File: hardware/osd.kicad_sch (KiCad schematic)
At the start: 0 parts

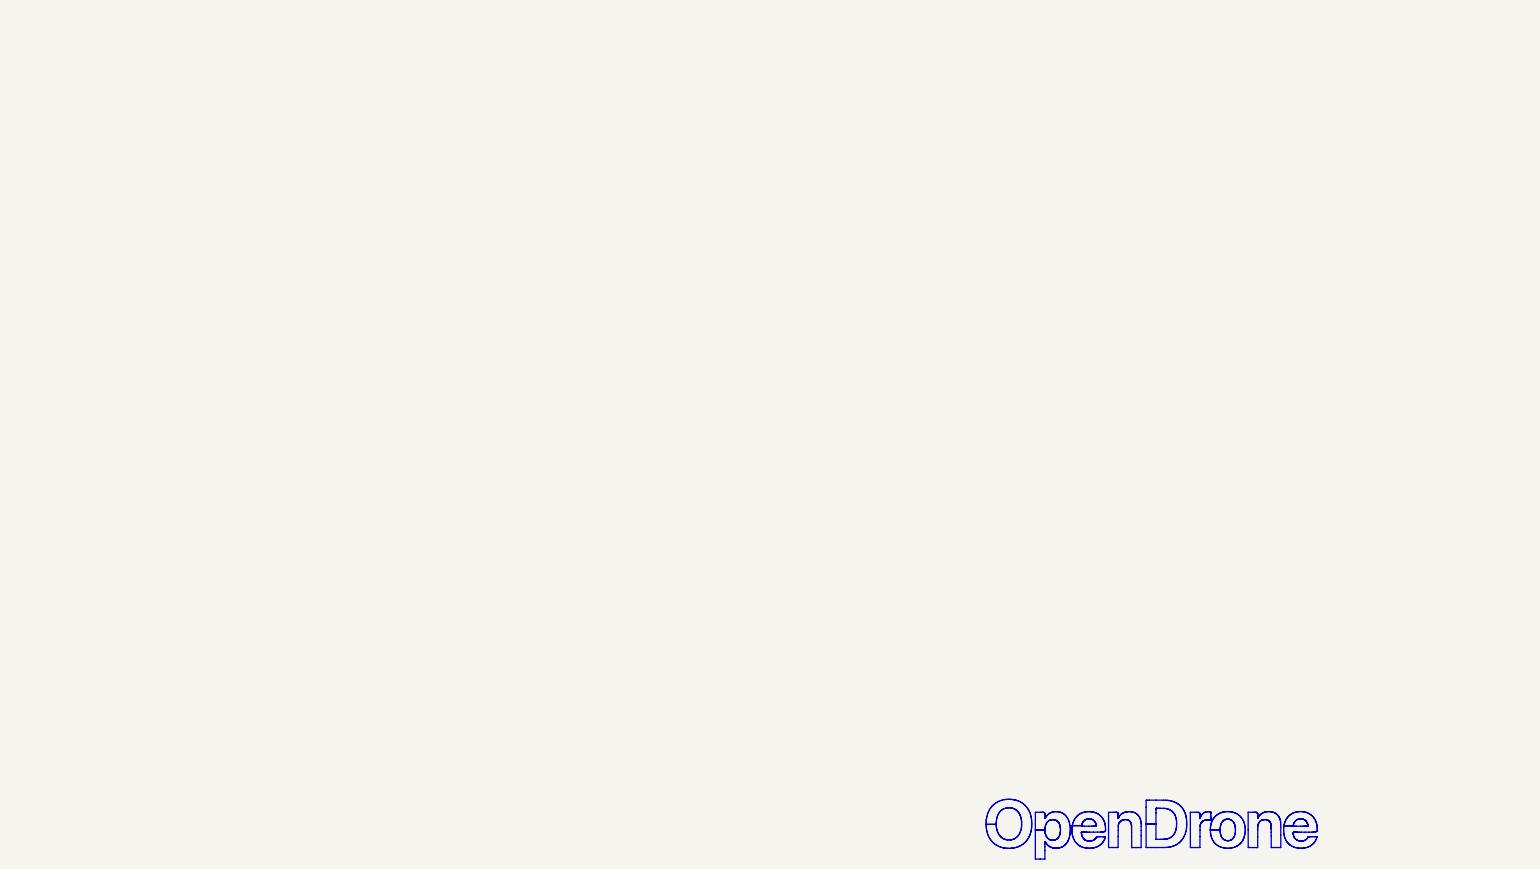
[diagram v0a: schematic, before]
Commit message: schematic: rx (ESP32-PICO-V3 + SX1281 + Wi-Fi antenna + boot button), blackbox and osd sheets drawn
Co-Authored-By: Claude Opus 5.5 <noreply@anthropic.com>
Claude-Session: https://claude.ai/code/session_01RFaS5jnC9tnPam9GBgmGnG
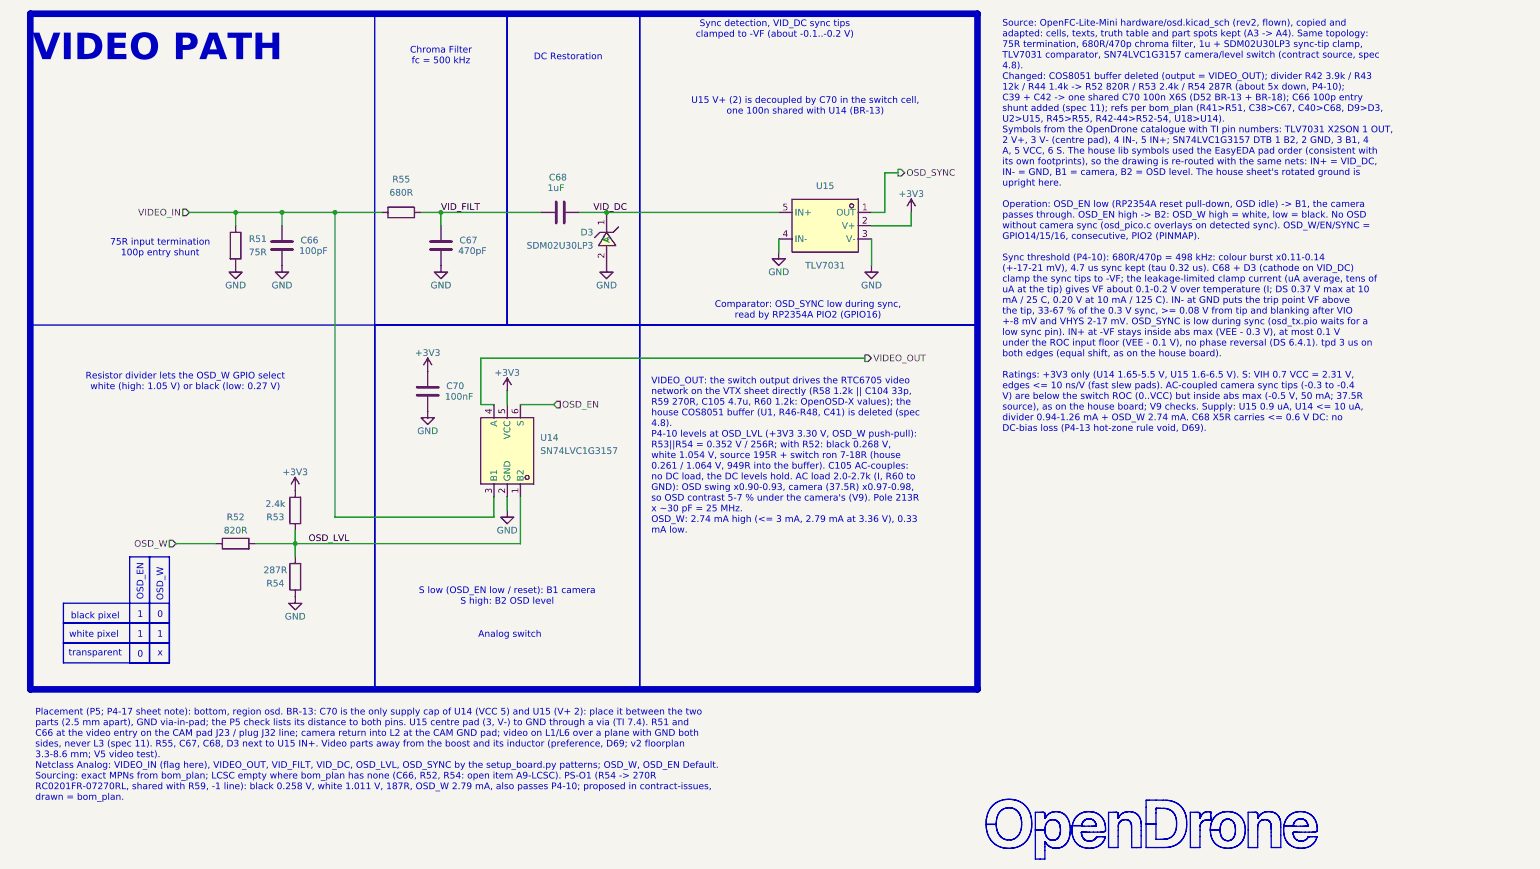
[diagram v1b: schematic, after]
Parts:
- added C66: 100pF, lib:C_0201_0603Metric_W, symbol Device:C
- added C67: 470pF, lib:C_0201_0603Metric_W, symbol Device:C
- added C68: 1uF, lib:C_0201_0603Metric_W, symbol Device:C
- added C70: 100nF, lib:C_0201_0603Metric_W, symbol Device:C
- added D3: SDM02U30LP3, lib:X3-DFN0603-2_L0.6-W0.3-RD_W, symbol OpenDrone:SDM02U30LP3-7B
- added R51: 75R, lib:R_0201_0603Metric_W, symbol Device:R
- added R52: 820R, lib:R_0201_0603Metric_W, symbol Device:R
- added R53: 2.4k, lib:R_0201_0603Metric_W, symbol Device:R
- added R54: 287R, lib:R_0201_0603Metric_W, symbol Device:R
- added R55: 680R, lib:R_0201_0603Metric_W, symbol Device:R
- added U14: SN74LVC1G3157, lib:X2SON-6_L1.0-W0.8-BL_Dense, symbol OpenDrone:SN74LVC1G3157DTBR
- added U15: TLV7031, lib:X2SON-4_L0.8-W0.8-P0.48-TL-A_Dense, symbol OpenDrone:TLV7031DPWR
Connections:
- new net +3V3: C70.1, R53.2, U14.5 (VCC), U15.2 (V+)
- new net GND: C66.2, C67.2, C70.2, D3.2 (A), R51.2, R54.1, U14.2 (GND), U15.3 (V-), U15.4 (IN-)
- new net OSD_EN: U14.6 (S)
- new net OSD_LVL: R52.2, R53.1, R54.2, U14.1 (B2)
- new net OSD_SYNC: U15.1 (OUT)
- new net OSD_W: R52.1
- new net VIDEO_IN: C66.1, R51.1, R55.2, U14.3 (B1)
- new net VIDEO_OUT: U14.4 (A)
- new net VID_DC: C68.2, D3.1 (C), U15.5 (IN+)
- new net VID_FILT: C67.1, C68.1, R55.1
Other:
- note added: "0"
- note added: "1"
- note added: "75R input termination 100p entry shunt"
- note added: "Analog switch"
- note added: "Chroma Filter fc = 500 kHz"
- note added: "Comparator: OSD_SYNC low during sync, read by RP2354A PIO2 (GPIO16)"
- note added: "DC Restoration"
- note added: "OSD_EN"
- note added: "OSD_W"
- note added: "Resistor divider lets the OSD_W GPIO select white (high: 1.05 V) or black (low: 0.27 V)"
- note added: "S low (OSD_EN low / reset): B1 camera S high: B2 OSD level"
- note added: "Sync detection, VID_DC sync tips clamped to -VF (about -0.1..-0.2 V)"
- note added: "U15 V+ (2) is decoupled by C70 in the switch cell, one 100n shared with U14 (BR-13)"
- note added: "VIDEO PATH"
- note added: "black pixel"
- note added: "transparent"
- note added: "white pixel"
- note added: "x"

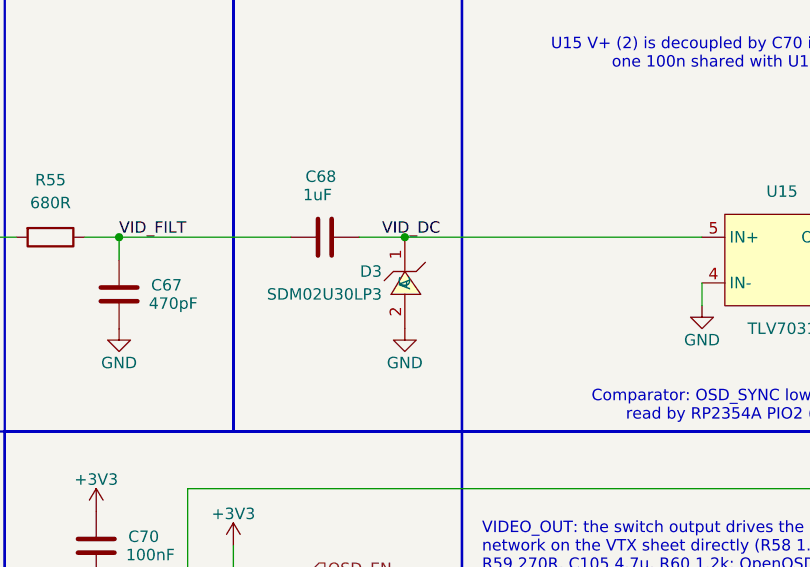
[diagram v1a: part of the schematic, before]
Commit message: wip: schematic integration in progress (saved after container restart)
Co-Authored-By: Claude Opus 5.5 <noreply@anthropic.com>
Claude-Session: https://claude.ai/code/session_01RFaS5jnC9tnPam9GBgmGnG
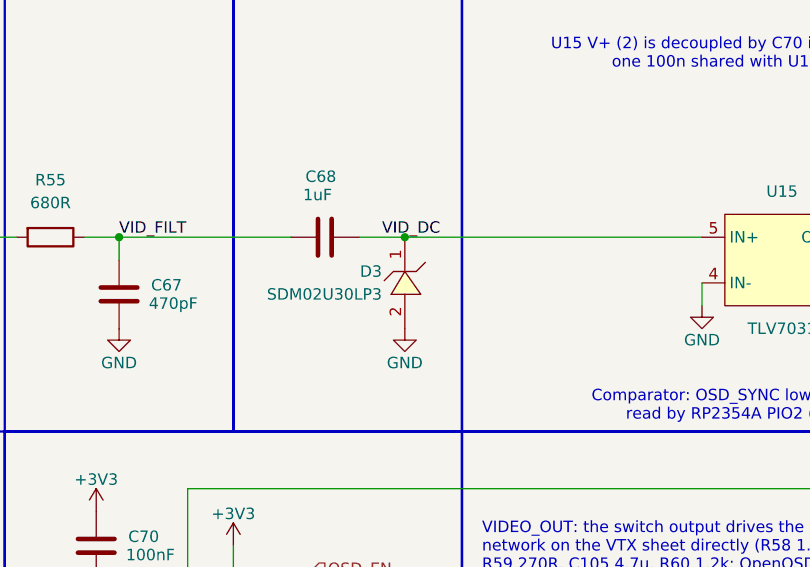
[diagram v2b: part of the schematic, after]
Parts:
- D3: symbol OpenDrone:SDM02U30LP3-7B -> lib:SDM02U30LP3-7B
- U14: symbol OpenDrone:SN74LVC1G3157DTBR -> lib:SN74LVC1G3157DTBR
- U15: symbol OpenDrone:TLV7031DPWR -> lib:TLV7031DPWR
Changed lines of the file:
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@@
 		(in_pos_files no)
 		(dnp no)
-		(property "Reference" "#PWR1005"
+		(property "Reference" "#PWR142"
 			(at 158.75 69.85 0)
 			(hide yes)
@@
 			(project "OpenAIO-Whoop"
 				(path "/2c3a7206-1e66-4d43-a02f-491225e20dd6/d622c956-8c4e-5ac1-b8c4-8a8024f124d6"
-					(reference "#PWR1005")
+					(reference "#PWR142")
 					(unit 1)
 				)
@@
 	)
 	(symbol
-		(lib_id "OpenDrone:SDM02U30LP3-7B")
+		(lib_id "lib:SDM02U30LP3-7B")
 		(at 125.73 60.96 270)
 		(unit 1)
@@
 		(in_pos_files no)
 		(dnp no)
-		(property "Reference" "#PWR1001"
+		(property "Reference" "#PWR143"
 			(at 54.61 72.39 0)
 			(hide yes)
@@
 			(project "OpenAIO-Whoop"
 				(path "/2c3a7206-1e66-4d43-a02f-491225e20dd6/d622c956-8c4e-5ac1-b8c4-8a8024f124d6"
-					(reference "#PWR1001")
+					(reference "#PWR143")
 					(unit 1)
 				)
@@
 		(in_pos_files no)
 		(dnp no)
-		(property "Reference" "#PWR1010"
+		(property "Reference" "#PWR152"
 			(at 106.68 119.38 0)
 			(hide yes)
@@
 			(project "OpenAIO-Whoop"
 				(path "/2c3a7206-1e66-4d43-a02f-491225e20dd6/d622c956-8c4e-5ac1-b8c4-8a8024f124d6"
-					(reference "#PWR1010")
+					(reference "#PWR152")
 					(unit 1)
 				)
@@
 		(in_pos_files no)
 		(dnp no)
-		(property "Reference" "#PWR1002"
+		(property "Reference" "#PWR144"
 			(at 63.5 72.39 0)
 			(hide yes)
@@
 			(project "OpenAIO-Whoop"
 				(path "/2c3a7206-1e66-4d43-a02f-491225e20dd6/d622c956-8c4e-5ac1-b8c4-8a8024f124d6"
-					(reference "#PWR1002")
+					(reference "#PWR144")
 					(unit 1)
 				)
@@
 		(in_pos_files no)
 		(dnp no)
-		(property "Reference" "#PWR1009"
+		(property "Reference" "#PWR153"
 			(at 66.04 135.89 0)
 			(hide yes)
@@
 			(project "OpenAIO-Whoop"
 				(path "/2c3a7206-1e66-4d43-a02f-491225e20dd6/d622c956-8c4e-5ac1-b8c4-8a8024f124d6"
-					(reference "#PWR1009")
+					(reference "#PWR153")
 					(unit 1)
 				)
@@
 		(in_pos_files no)
 		(dnp no)
-		(property "Reference" "#PWR1007"
+		(property "Reference" "#PWR141"
 			(at 184.15 59.69 0)
 			(hide yes)
@@
 			(project "OpenAIO-Whoop"
 				(path "/2c3a7206-1e66-4d43-a02f-491225e20dd6/d622c956-8c4e-5ac1-b8c4-8a8024f124d6"
-					(reference "#PWR1007")
+					(reference "#PWR141")
 					(unit 1)
 				)
@@
 	)
 	(symbol
-		(lib_id "OpenDrone:TLV7031DPWR")
+		(lib_id "lib:TLV7031DPWR")
 		(at 167.64 58.42 0)
 		(mirror y)
@@
 		(in_pos_files no)
 		(dnp no)
-		(property "Reference" "#PWR1011"
+		(property "Reference" "#PWR149"
 			(at 106.68 93.98 0)
 			(hide yes)
@@
 			(project "OpenAIO-Whoop"
 				(path "/2c3a7206-1e66-4d43-a02f-491225e20dd6/d622c956-8c4e-5ac1-b8c4-8a8024f124d6"
-					(reference "#PWR1011")
+					(reference "#PWR149")
 					(unit 1)
 				)
@@
 		(in_pos_files no)
 		(dnp no)
-		(property "Reference" "#PWR1008"
+		(property "Reference" "#PWR151"
 			(at 66.04 113.03 0)
 			(hide yes)
@@
 			(project "OpenAIO-Whoop"
 				(path "/2c3a7206-1e66-4d43-a02f-491225e20dd6/d622c956-8c4e-5ac1-b8c4-8a8024f124d6"
-					(reference "#PWR1008")
+					(reference "#PWR151")
 					(unit 1)
 				)
@@
 	)
 	(symbol
-		(lib_id "OpenDrone:SN74LVC1G3157DTBR")
+		(lib_id "lib:SN74LVC1G3157DTBR")
 		(at 106.68 101.6 270)
 		(mirror x)
@@
 		(in_pos_files no)
 		(dnp no)
-		(property "Reference" "#PWR1004"
+		(property "Reference" "#PWR146"
 			(at 125.73 72.39 0)
 			(hide yes)
@@
 			(project "OpenAIO-Whoop"
 				(path "/2c3a7206-1e66-4d43-a02f-491225e20dd6/d622c956-8c4e-5ac1-b8c4-8a8024f124d6"
-					(reference "#PWR1004")
+					(reference "#PWR146")
 					(unit 1)
 				)
@@
 		(in_pos_files no)
 		(dnp no)
-		(property "Reference" "#PWR1013"
+		(property "Reference" "#PWR150"
 			(at 91.44 100.33 0)
 			(hide yes)
@@
 			(project "OpenAIO-Whoop"
 				(path "/2c3a7206-1e66-4d43-a02f-491225e20dd6/d622c956-8c4e-5ac1-b8c4-8a8024f124d6"
-					(reference "#PWR1013")
+					(reference "#PWR150")
 					(unit 1)
 				)
@@
 		(in_pos_files no)
 		(dnp no)
-		(property "Reference" "#PWR1012"
+		(property "Reference" "#PWR148"
 			(at 91.44 90.17 0)
 			(hide yes)
@@
 			(project "OpenAIO-Whoop"
 				(path "/2c3a7206-1e66-4d43-a02f-491225e20dd6/d622c956-8c4e-5ac1-b8c4-8a8024f124d6"
-					(reference "#PWR1012")
+					(reference "#PWR148")
 					(unit 1)
 				)
@@
 		(in_pos_files no)
 		(dnp no)
-		(property "Reference" "#PWR1003"
+		(property "Reference" "#PWR145"
 			(at 93.98 72.39 0)
 			(hide yes)
@@
 			(project "OpenAIO-Whoop"
 				(path "/2c3a7206-1e66-4d43-a02f-491225e20dd6/d622c956-8c4e-5ac1-b8c4-8a8024f124d6"
-					(reference "#PWR1003")
+					(reference "#PWR145")
 					(unit 1)
 				)
@@
 		(in_pos_files no)
 		(dnp no)
-		(property "Reference" "#PWR1006"
+		(property "Reference" "#PWR147"
 			(at 176.53 72.39 0)
 			(hide yes)
@@
 			(project "OpenAIO-Whoop"
 				(path "/2c3a7206-1e66-4d43-a02f-491225e20dd6/d622c956-8c4e-5ac1-b8c4-8a8024f124d6"
-					(reference "#PWR1006")
-					(unit 1)
-				)
+					(reference "#PWR147")
+					(unit 1)
+				)
